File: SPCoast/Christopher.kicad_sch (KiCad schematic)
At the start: 72 parts, among them SW9813 813, SW9815 815, SW9817 817, SW9900 815A, SW9901 813, SW9902 817

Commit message: refactor(symbols): the CP field is CP Name on every trackplan symbol
One fact, which house an appliance or circuit stands in, had two field
names: CP Name on the House and PanelColumn, CP on 17 trackplan
symbols. Every CP is now CP Name, in the library and in each placed
symbol, by a text rename of the field name only (KiCad's update
symbols was not used; it resets per-instance fields).

Verified: fresh kicad-cli netlists before and after: 754 components on
both, 136 had CP, every field identical once CP is read as CP Name, no
CP left. lint_symbol_fields: 100 symbols, 0 errors, 0 warnings.

Co-Authored-By: Claude Opus 5.5 <noreply@anthropic.com>
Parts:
- B9004, B9007, SW9817, TC9001, TC9002: CP Christopher South -> (none); CP Name (none) -> Christopher South
- B9005, B9006, SW9813, SW9815, SW9900, TC9003, TC9004, TC9005: CP Christopher North -> (none); CP Name (none) -> Christopher North
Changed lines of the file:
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@@
 			)
 		)
-		(property "CP" "Christopher North"
+		(property "CP Name" "Christopher North"
 			(at 55.88 102.235 0)
 			(show_name no)
@@
 			)
 		)
-		(property "CP" "Christopher North"
+		(property "CP Name" "Christopher North"
 			(at 132.08 104.775 0)
 			(show_name no)
@@
 			)
 		)
-		(property "CP" "Christopher North"
+		(property "CP Name" "Christopher North"
 			(at 83.82 95.885 0)
 			(show_name no)
@@
 			)
 		)
-		(property "CP" "Christopher South"
+		(property "CP Name" "Christopher South"
 			(at 195.58 69.85 0)
 			(show_name no)
@@
 			)
 		)
-		(property "CP" "Christopher North"
+		(property "CP Name" "Christopher North"
 			(at 130.81 118.745 0)
 			(show_name no)
@@
 			)
 		)
-		(property "CP" "Christopher North"
+		(property "CP Name" "Christopher North"
 			(at 72.39 64.77 0)
 			(show_name no)
@@
 			)
 		)
-		(property "CP" "Christopher North"
+		(property "CP Name" "Christopher North"
 			(at 170.18 62.865 0)
 			(show_name no)
@@
 			)
 		)
-		(property "CP" "Christopher South"
+		(property "CP Name" "Christopher South"
 			(at 210.82 69.215 0)
 			(show_name no)
@@
 			)
 		)
-		(property "CP" "Christopher North"
+		(property "CP Name" "Christopher North"
 			(at 71.12 97.79 0)
 			(show_name no)
@@
 			)
 		)
-		(property "CP" "Christopher South"
+		(property "CP Name" "Christopher South"
 			(at 210.82 102.235 0)
 			(show_name no)
@@
 			)
 		)
-		(property "CP" "Christopher South"
+		(property "CP Name" "Christopher South"
 			(at 196.85 102.87 0)
 			(show_name no)
@@
 			)
 		)
-		(property "CP" "Christopher South"
+		(property "CP Name" "Christopher South"
 			(at 184.15 95.885 0)
 			(show_name no)
@@
 			)
 		)
-		(property "CP" "Christopher North"
+		(property "CP Name" "Christopher North"
 			(at 55.88 69.215 0)
 			(show_name no)

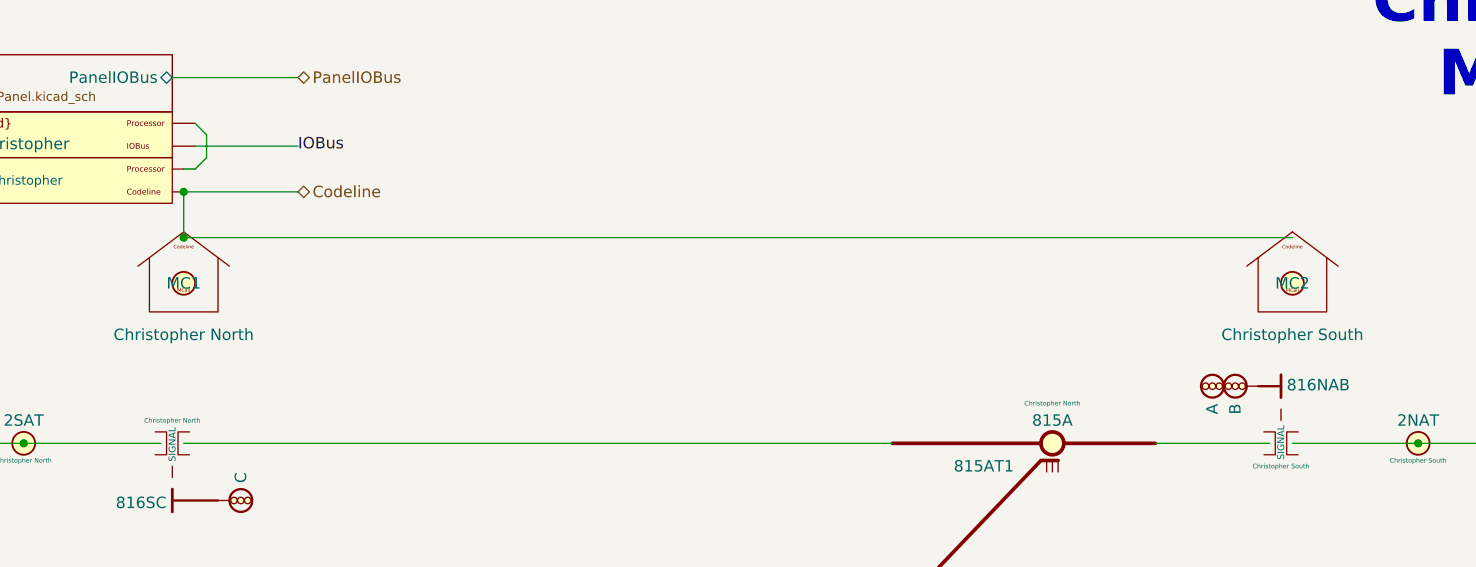
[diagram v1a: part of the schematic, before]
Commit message: feat(spcoast): per-pin token fields on the panels, lamp Indication expressions, maintainer calls named 1MC
Applies the symbol rulings of 2026-10-28 to every sheet: the lib_symbols
caches of the changed symbols are the library's copies (this also clears
the stale PanelMCall and MaintainerCall caches), and every placed
instance gets the new hidden Control.*/Indication.* fields, loses
PanelLock Invert, and PanelMCall's whole-symbol Control and Indication
(Pin.MCK binary). Model lamps' IndicationToken becomes Indication: each
comma-separated circuit gets its K, qualifiers kept, joined with " | "
(795T1,01T,799T1 -> 795T1K | 01TK | 799T1K).

Maintainer calls in Christopher (1, 2), Corporal, Luchessa and Sargent
follow Gilroy Interchange (5dad54f): Value MC<n> -> <n>, Name ${Value}MC,
and the separate PanelMCall-Lamp is replaced by unit 2 of the same
PanelMCall at the old lamp's position, so its MCK pin sits where the
LAMP pin was. The old lamps' Column pin touched PanelColumn pin 8
directly (no wire); that pin is now unconnected, as on Gilroy
Interchange. Gilroy Interchange's local MaintainerCall_1 cache and its
two trackplan calls lose Indication.

Verified: fresh netlist before/after: components 752 -> 747 (the five
lamps), nets 1028 -> 1028; each old LAMP-pin net now holds the lever's
unit-2 MCK pin (pin 3) on the same expander pin (B1, pin 9); the levers'
nets are renamed only (~{S} -> ~{MCS}, unit suffix A); no other net
changed. Every field difference is an intended one. ERC 18 -> 1
violations (lib_symbol_mismatch 17 -> 0; pre-existing Sargent AUX1
pin_not_connected remains).

Co-Authored-By: Claude Opus 5.5 <noreply@anthropic.com>
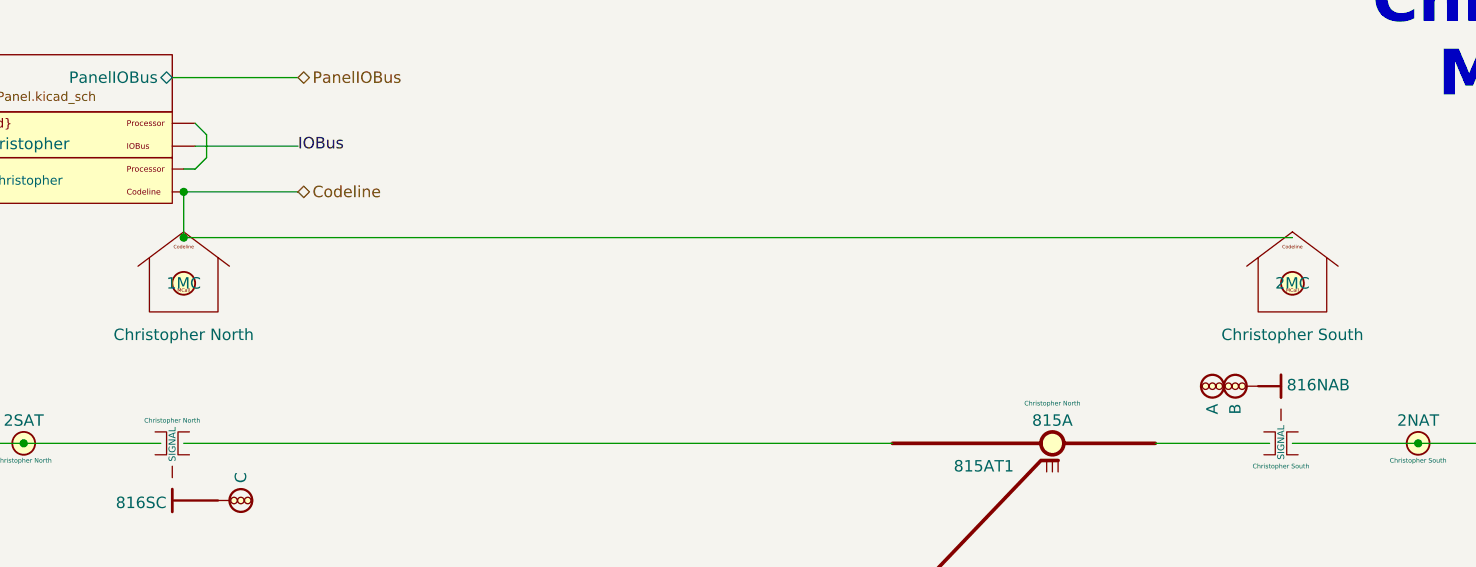
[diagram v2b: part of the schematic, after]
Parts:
- MC9001: value MC1 -> 1; Name ${Value} -> ${Value}MC
- MC9002: value MC2 -> 2; Name ${Value} -> ${Value}MC
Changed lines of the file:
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@@
 			)
 		)
-		(property "Value" "MC1"
+		(property "Value" "1"
 			(at 73.66 49.53 0)
+			(hide yes)
 			(show_name no)
 			(do_not_autoplace no)
@@
 			)
 		)
-		(property "Name" "${Value}"
+		(property "Name" "${Value}MC"
 			(at 73.66 49.53 0)
-			(hide yes)
 			(show_name no)
 			(do_not_autoplace no)
@@
 			)
 		)
-		(property "Value" "MC2"
+		(property "Value" "2"
 			(at 196.85 49.53 0)
+			(hide yes)
 			(show_name no)
 			(do_not_autoplace no)
@@
 			)
 		)
-		(property "Name" "${Value}"
+		(property "Name" "${Value}MC"
 			(at 196.85 49.53 0)
-			(hide yes)
-			(show_name no)
-			(do_not_autoplace no)
+			(show_name no)
+			(do_not_autoplace no)

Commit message: feat(symbols,spcoast): track circuits state their Indication; virtual circuits list Members
The owner's edit, 2026-10-29. Every Track Circuit symbol (plain, RED,
Yellow, Virtual) carries Indication=${Name}K: the token a local circuit
reports and a remote consumer (Sargent's Corporal:2NAT) consumes, so
both sides state it and match token to token. Track Circuit_Virtual's
IndicationToken becomes Members (the local circuits it is made of, not
tokens), with Display=${Value}: [${Members}]. Sargent's HBA gets a
no-connect on its unused pin. The panel sheets are re-saved by KiCad
with no field changes.

Verified:
- netlist field diff against 69e87ec: 747 components, none added or
  removed; the only changes are Indication added on 63 track circuits
  (26 Track Circuit, 35 Yellow, 2 Virtual) and IndicationToken renamed
  to Members on TC15032 and TC15034
- ERC: 0 violations (was 1, Sargent AUX1 pin_not_connected)
- Subdivision lint_symbol_fields: 100 symbols, 0 errors, 0 warnings
- Subdivision fresh compile: 0 errors, 0 warnings, 8 info, 2 missing;
  consumer.legacy_token no longer fires

Co-Authored-By: Claude Opus 5.5 <noreply@anthropic.com>
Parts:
- TC9001, TC9002, TC9003, TC9004, TC9005: Indication (none) -> ${Name}K
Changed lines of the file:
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@@
 		)
 		(property "Value" "1SAT"
-			(at 55.88 97.79 0)
+			(at 55.88 102.87 0)
+			(hide yes)
 			(show_name no)
-			(do_not_autoplace no)
+			(do_not_autoplace yes)
 			(effects
 				(font
@@
 			)
 		)
+		(property "Indication" "${Name}K"
+			(at 57.15 106.68 0)
+			(hide yes)
+			(show_name no)
+			(do_not_autoplace no)
+			(effects
+				(font
+					(size 1.27 1.27)
+				)
+			)
+		)
 		(pin "1"
 		)
@@
 		)
 		(property "Value" "01T"
-			(at 130.81 114.3 0)
+			(at 130.81 119.38 0)
+			(hide yes)
 			(show_name no)
-			(do_not_autoplace no)
+			(do_not_autoplace yes)
 			(effects
 				(font
@@
 			)
 		)
+		(property "Indication" "${Name}K"
+			(at 132.08 123.19 0)
+			(hide yes)
+			(show_name no)
+			(do_not_autoplace no)
+			(effects
+				(font
+					(size 1.27 1.27)
+				)
+			)
+		)
 		(pin "1"
 		)
@@
 		)
 		(property "Value" "2NAT"
-			(at 210.82 64.77 0)
+			(at 210.82 69.85 0)
+			(hide yes)
 			(show_name no)
-			(do_not_autoplace no)
+			(do_not_autoplace yes)
 			(effects
 				(font
@@
 			)
 		)
+		(property "Indication" "${Name}K"
+			(at 212.09 73.66 0)
+			(hide yes)
+			(show_name no)
+			(do_not_autoplace no)
+			(effects
+				(font
+					(size 1.27 1.27)
+				)
+			)
+		)
 		(pin "1"
 		)
@@
 		)
 		(property "Value" "1NAT"
-			(at 210.82 97.79 0)
+			(at 210.82 102.87 0)
+			(hide yes)
 			(show_name no)
-			(do_not_autoplace no)
+			(do_not_autoplace yes)
 			(effects
 				(font
@@
 			)
 		)
+		(property "Indication" "${Name}K"
+			(at 212.09 106.68 0)
+			(hide yes)
+			(show_name no)
+			(do_not_autoplace no)
+			(effects
+				(font
+					(size 1.27 1.27)
+				)
+			)
+		)
 		(pin "1"
 		)
@@
 		)
 		(property "Value" "2SAT"
-			(at 55.88 64.77 0)
+			(at 55.88 69.85 0)
+			(hide yes)
 			(show_name no)
-			(do_not_autoplace no)
+			(do_not_autoplace yes)
 			(effects
 				(font
@@
 			(hide yes)
 			(show_name no)
+			(do_not_autoplace no)
+			(effects
+				(font
+					(size 1.27 1.27)
+				)
+			)
+		)
+		(property "Indication" "${Name}K"
+			(at 57.15 73.66 0)
+			(hide yes)
+			(show_name no)

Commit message: feat(symbols): switches and field lamps state their indication token
A switch states its OS circuit's token, Indication=${TC}K, on Switch_Dual,
Switch_Lock, Switch_Powered, Switch_Powered_Diag, Switch_Powered_Small and
Derail_TC; symbols with no TC (Derail, Switch_Manual, Switch_Manual_Sensed,
Switch_Powered_NO_TC) carry the field present and empty. The AUXILIARY field
lamp states Indication=${Name}K. The four NFLK/SFLK lamps in Luchessa and
Watsonville are renamed NFL/SFL, so their tokens stay NFLK/SFLK. The
sheets are updated from the library.

Verified:
- fresh kicad-cli netlist vs HEAD 6ce30b3: 747 components each, 46 field
  changes: 31 switch/derail Indication, HBA Indication=HBAK, the four
  NFL/SFL renames with their Indication, and MC5001's library entry name
  (MaintainerCall_1 -> MaintainerCall); nothing else
- kicad-cli ERC: 0 violations
- tools/contract/lint_symbol_fields.py: 100 symbols, 0 errors, 0 warnings
- compile_layout.py: 0 errors, 0 warnings, 8 info, 2 missing (unchanged)

Co-Authored-By: Claude Opus 5.5 <noreply@anthropic.com>
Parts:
- SW9813, SW9815, SW9817, SW9900: Indication (none) -> ${TC}K
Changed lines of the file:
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@@
 			)
 		)
+		(property "Indication" "${TC}K"
+			(at 132.08 100.33 0)
+			(hide yes)
+			(show_name no)
+			(do_not_autoplace no)
+			(effects
+				(font
+					(size 1.27 1.27)
+				)
+			)
+		)
 		(pin "2"
 		)
@@
 			)
 		)
+		(property "Indication" "${TC}K"
+			(at 83.82 100.33 0)
+			(hide yes)
+			(show_name no)
+			(do_not_autoplace no)
+			(effects
+				(font
+					(size 1.27 1.27)
+				)
+			)
+		)
 		(pin "3"
 		)
@@
 			)
 		)
+		(property "Indication" "${TC}K"
+			(at 170.18 67.31 0)
+			(hide yes)
+			(show_name no)
+			(do_not_autoplace no)
+			(effects
+				(font
+					(size 1.27 1.27)
+				)
+			)
+		)
 		(pin "2"
 		)
@@
 			(hide yes)
 			(show_name no)
+			(do_not_autoplace no)
+			(effects
+				(font
+					(size 1.27 1.27)
+				)
+			)
+		)
+		(property "Indication" "${TC}K"
+			(at 184.15 100.33 0)
+			(hide yes)
+			(show_name no)
